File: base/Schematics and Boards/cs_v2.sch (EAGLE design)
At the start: 72 parts, among them J101 J-JTAG-CORTEX-NEEDLE6, J301 HIROSE-DF40_44-PIN_CONNECTORS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, J302 HIROSE-DF40_30-PIN_CONNECTORS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, Q201 FK3303010L, Q202 FK3303010L, Q203 FK3303010L, Q204 DMG3415UFY4Q-7, U1 AT25SF641-MHB-T, U101 ATSAMD51, U201 COULOMB-MAX17262, U202 CUS520H3F, U203 MAX77827BEWC+T, U204 SENSOR-SI7006, U205 LOADSWITCH-MIC94164, U206 LOADSWITCH-MIC94164, Y101 16M, Y102 ABS07-32.768KHZ-9-T

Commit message: Minor sh changes; placed compressed power subsys, gitignore temp files
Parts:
- added JP1: JUMPER-SMT_3_1-NC_PASTE_NO-SILK, SparkFun-Jumpers:JUMPER-SMT_3_1-NC_PASTE_NO-SILK
- added TP1, TP10, TP2, TP5, TP6, TP7, TP8, TP9: TPTP08R, TestPoints:TPTP08R
- C206, C208: SPICEPREFIX (none) -> C
- R208: SPICEPREFIX (none) -> R
- U205: SPICEPREFIX (none) -> E
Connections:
- net N$18 renamed +3V3_DTR_SENSE
- net N$19 renamed +3V3_PROC_SENSE
- new net VDD_SW_IN: JP1.2, S201.P
- net +3V3_DTR: now also TP6.TP
- net +3V3_PROC: now also TP5.TP
- net +3V3_STOR: now also TP8.TP
- net +3V3_TEMP: now also TP7.TP
- net +3V7_BATT: now also JP1.1
- net CC_IN: now also S201.S; no longer S201.O
- net DTR_MASTER_I2C_SCL: now also TP10.TP
- net DTR_MASTER_I2C_SDA: now also TP9.TP
- net N$1: now also TP1.TP
- net VDD_SW: now also JP1.3; no longer S201.P
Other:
- note added: "Provide info on board health (humitidy/temp) and info to help with crystal frequency offset resulting from temperature; should be placed near XTALs"
- note removed: "Idea: put similar pins (rather than SERCOM buses) right next to each other to make passthrough easier for dtr boards"
- note removed: "Provide info on board health (humitidy/temp) and info to help with crystal frequency offset resulting from temperature"
- moved on the sheet: C201, C203, S201, U201, U202

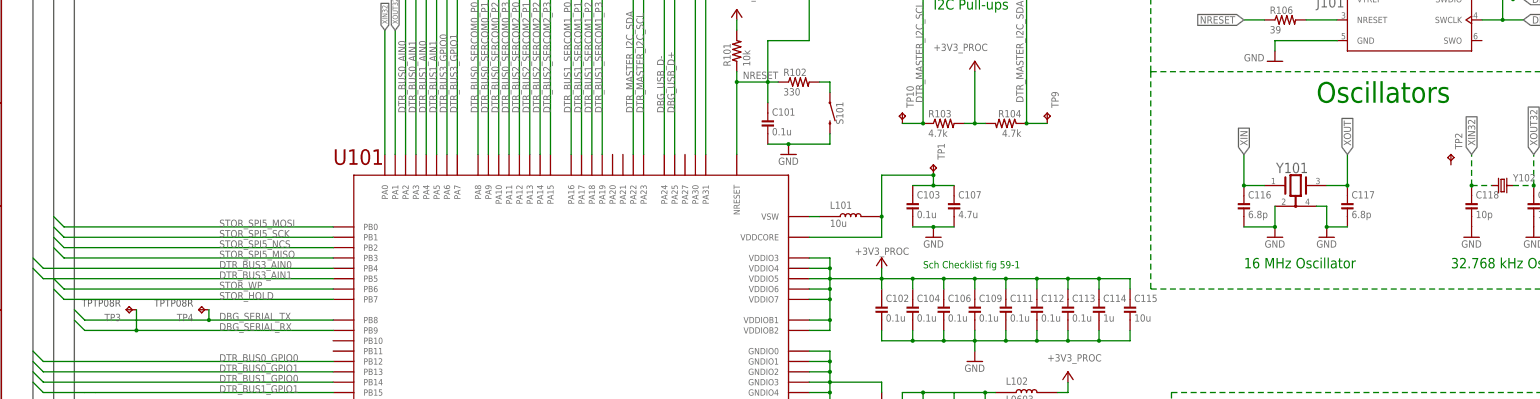
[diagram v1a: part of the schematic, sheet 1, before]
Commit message: Board placement for 1in x 1in. Unrouted
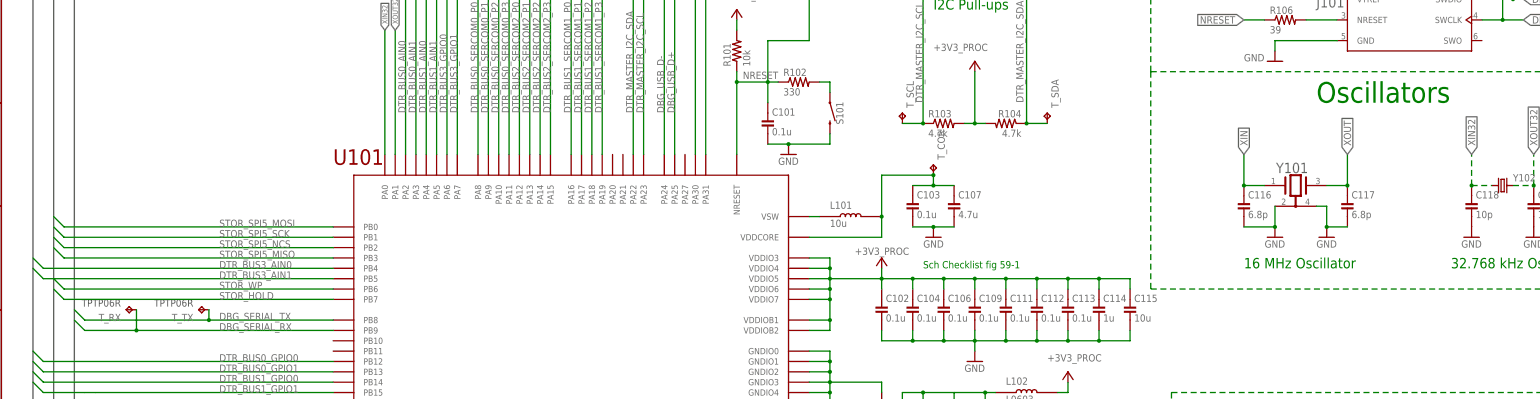
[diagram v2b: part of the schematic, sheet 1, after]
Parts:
- removed TP1, TP10, TP2, TP3, TP4, TP5, TP6, TP7, TP8, TP9: TPTP08R, TestPoints:TPTP08R
- added T_COR, T_CPU, T_DTR, T_RX, T_SCL, T_SDA, T_STR, T_TMP, T_TX: TPTP06R, TestPoints:TPTP06R
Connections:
- net N$2 renamed VSW
- net N$3 renamed VDDANA
- removed net N$1: C103.1, C107.1, L101.2, TP1.TP, U101.VDDCORE
- new net VDDCORE: C103.1, C107.1, L101.2, T_COR.TP, U101.VDDCORE
- net +3V3_DTR: now also T_DTR.TP; no longer TP6.TP
- net +3V3_PROC: now also T_CPU.TP; no longer TP5.TP
- net +3V3_STOR: now also T_STR.TP; no longer TP8.TP
- net +3V3_TEMP: now also T_TMP.TP; no longer TP7.TP
- net DBG_SERIAL_RX: now also T_RX.TP; no longer TP3.TP
- net DBG_SERIAL_TX: now also T_TX.TP; no longer TP4.TP
- net DTR_MASTER_I2C_SCL: now also T_SCL.TP; no longer TP10.TP
- net DTR_MASTER_I2C_SDA: now also T_SDA.TP; no longer TP9.TP
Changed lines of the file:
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@@
 <part name="+3V5" library="Supplies" deviceset="+3V3" device=""/>
 <part name="GND18" library="Supplies" deviceset="GND" device=""/>
-<part name="TP3" library="TestPoints" deviceset="TP" device="TP08R" package3d_urn="urn:adsk.eagle:package:27956/1"/>
-<part name="TP4" library="TestPoints" deviceset="TP" device="TP08R" package3d_urn="urn:adsk.eagle:package:27956/1"/>
+<part name="T_RX" library="TestPoints" deviceset="TP" device="TP06R" package3d_urn="urn:adsk.eagle:package:27954/1" value="TPTP06R"/>
+<part name="T_TX" library="TestPoints" deviceset="TP" device="TP06R" package3d_urn="urn:adsk.eagle:package:27954/1" value="TPTP06R"/>
 <part name="R106" library="Resistors" deviceset="R-" device="0402" value="39">
 <attribute name="PART_NO" value="ERJ-2GEJ390X"/>
@@
 <part name="GND14" library="Supplies" deviceset="GND" device=""/>
 <part name="JP1" library="SparkFun-Jumpers" deviceset="JUMPER-SMT_3_1-NC_PASTE" device="_NO-SILK" package3d_urn="urn:adsk.eagle:package:39291/1"/>
-<part name="TP1" library="TestPoints" deviceset="TP" device="TP08R" package3d_urn="urn:adsk.eagle:package:27956/1"/>
-<part name="TP2" library="TestPoints" deviceset="TP" device="TP08R" package3d_urn="urn:adsk.eagle:package:27956/1"/>
-<part name="TP5" library="TestPoints" deviceset="TP" device="TP08R" package3d_urn="urn:adsk.eagle:package:27956/1"/>
-<part name="TP6" library="TestPoints" deviceset="TP" device="TP08R" package3d_urn="urn:adsk.eagle:package:27956/1"/>
-<part name="TP7" library="TestPoints" deviceset="TP" device="TP08R" package3d_urn="urn:adsk.eagle:package:27956/1"/>
-<part name="TP8" library="TestPoints" deviceset="TP" device="TP08R" package3d_urn="urn:adsk.eagle:package:27956/1">
+<part name="T_COR" library="TestPoints" deviceset="TP" device="TP06R" package3d_urn="urn:adsk.eagle:package:27954/1" value="TPTP06R"/>
+<part name="T_CPU" library="TestPoints" deviceset="TP" device="TP06R" package3d_urn="urn:adsk.eagle:package:27954/1" value="TPTP06R"/>
+<part name="T_DTR" library="TestPoints" deviceset="TP" device="TP06R" package3d_urn="urn:adsk.eagle:package:27954/1" value="TPTP06R"/>
+<part name="T_TMP" library="TestPoints" deviceset="TP" device="TP06R" package3d_urn="urn:adsk.eagle:package:27954/1" value="TPTP06R"/>
+<part name="T_STR" library="TestPoints" deviceset="TP" device="TP06R" package3d_urn="urn:adsk.eagle:package:27954/1" value="TPTP06R">
 <attribute name="SPICEPREFIX" value="X"/>
 </part>
-<part name="TP9" library="TestPoints" deviceset="TP" device="TP08R" package3d_urn="urn:adsk.eagle:package:27956/1"/>
-<part name="TP10" library="TestPoints" deviceset="TP" device="TP08R" package3d_urn="urn:adsk.eagle:package:27956/1"/>
+<part name="T_SDA" library="TestPoints" deviceset="TP" device="TP06R" package3d_urn="urn:adsk.eagle:package:27954/1" value="TPTP06R"/>
+<part name="T_SCL" library="TestPoints" deviceset="TP" device="TP06R" package3d_urn="urn:adsk.eagle:package:27954/1" value="TPTP06R"/>
 </parts>
 <sheets>
@@
 <attribute name="VALUE" x="307.34" y="213.36" size="1.778" layer="96"/>
 </instance>
-<instance part="TP3" gate="G$1" x="33.02" y="152.4" smashed="yes" rot="R90">
+<instance part="T_RX" gate="G$1" x="33.02" y="152.4" smashed="yes" rot="R90">
 <attribute name="NAME" x="31.75" y="151.384" size="1.778" layer="95" rot="R180"/>
 <attribute name="VALUE" x="31.75" y="154.94" size="1.778" layer="97" rot="R180"/>
 </instance>
-<instance part="TP4" gate="G$1" x="50.8" y="152.4" smashed="yes" rot="R90">
+<instance part="T_TX" gate="G$1" x="50.8" y="152.4" smashed="yes" rot="R90">
 <attribute name="NAME" x="49.53" y="151.384" size="1.778" layer="95" rot="R180"/>
 <attribute name="VALUE" x="49.53" y="154.94" size="1.778" layer="97" rot="R180"/>
@@
 <attribute name="VALUE" x="363.22" y="63.5" size="1.778" layer="96"/>
 </instance>
-<instance part="TP1" gate="G$1" x="231.14" y="187.96" smashed="yes" rot="MR0">
+<instance part="T_COR" gate="G$1" x="231.14" y="187.96" smashed="yes" rot="MR0">
 <attribute name="NAME" x="232.156" y="189.23" size="1.778" layer="95" rot="MR90"/>
 </instance>
-<instance part="TP2" gate="G$1" x="358.14" y="190.5" smashed="yes" rot="MR0">
-<attribute name="NAME" x="359.156" y="191.77" size="1.778" layer="95" rot="MR90"/>
-</instance>
-<instance part="TP9" gate="G$1" x="259.08" y="200.66" smashed="yes" rot="MR0">
+<instance part="T_SDA" gate="G$1" x="259.08" y="200.66" smashed="yes" rot="MR0">
 <attribute name="NAME" x="260.096" y="201.93" size="1.778" layer="95" rot="MR90"/>
 </instance>
-<instance part="TP10" gate="G$1" x="223.52" y="200.66" smashed="yes" rot="MR0">
+<instance part="T_SCL" gate="G$1" x="223.52" y="200.66" smashed="yes" rot="MR0">
 <attribute name="NAME" x="224.536" y="201.93" size="1.778" layer="95" rot="MR90"/>
 </instance>
@@
 </segment>
 </net>
-<net name="N$1" class="0">
+<net name="VDDCORE" class="0">
 <segment>
 <pinref part="U101" gate="G$1" pin="VDDCORE"/>
@@
 <wire x1="231.14" y1="185.42" x2="231.14" y2="182.88" width="0.1524" layer="91"/>
 <junction x="231.14" y="182.88"/>
-<pinref part="TP1" gate="G$1" pin="TP"/>
+<pinref part="T_COR" gate="G$1" pin="TP"/>
 <junction x="231.14" y="185.42"/>
 </segment>
 </net>
-<net name="N$2" class="0">
+<net name="VSW" class="0">
 <segment>
 <pinref part="U101" gate="G$1" pin="VSW"/>
@@
 </segment>
 </net>
-<net name="N$3" class="0">
+<net name="VDDANA" class="0">
 <segment>
 <pinref part="U101" gate="G$1" pin="VDDANA1"/>
@@
 <wire x1="53.34" y1="149.86" x2="22.86" y2="149.86" width="0.1524" layer="91"/>
 <wire x1="22.86" y1="149.86" x2="20.32" y2="152.4" width="0.1524" layer="91"/>
-<pinref part="TP4" gate="G$1" pin="TP"/>
+<pinref part="T_TX" gate="G$1" pin="TP"/>
 <wire x1="53.34" y1="149.86" x2="53.34" y2="152.4" width="0.1524" layer="91"/>
 <junction x="53.34" y="149.86"/>
@@
 <wire x1="35.56" y1="147.32" x2="22.86" y2="147.32" width="0.1524" layer="91"/>
 <wire x1="22.86" y1="147.32" x2="20.32" y2="149.86" width="0.1524" layer="91"/>
-<pinref part="TP3" gate="G$1" pin="TP"/>
+<pinref part="T_RX" gate="G$1" pin="TP"/>
 <wire x1="35.56" y1="147.32" x2="35.56" y2="152.4" width="0.1524" layer="91"/>
 <junction x="35.56" y="147.32"/>
@@
 <wire x1="254" y1="198.12" x2="259.08" y2="198.12" width="0.1524" layer="91"/>
 <junction x="254" y="198.12"/>
-<pinref part="TP9" gate="G$1" pin="TP"/>
+<pinref part="T_SDA" gate="G$1" pin="TP"/>
 </segment>
 </net>
@@
 <pinref part="R103" gate="G$1" pin="1"/>
 <label x="228.6" y="203.2" size="1.778" layer="95" rot="R90"/>
-<pinref part="TP10" gate="G$1" pin="TP"/>
+<pinref part="T_SCL" gate="G$1" pin="TP"/>
 <wire x1="228.6" y1="198.12" x2="223.52" y2="198.12" width="0.1524" layer="91"/>
 <junction x="228.6" y="198.12"/>
@@
 <attribute name="NAME" x="86.36" y="175.641" size="1.778" layer="95" font="vector" rot="MR0"/>
 </instance>
-<instance part="TP5" gate="G$1" x="350.52" y="190.5" smashed="yes" rot="MR0">
+<instance part="T_CPU" gate="G$1" x="350.52" y="190.5" smashed="yes" rot="MR0">
 <attribute name="NAME" x="351.536" y="191.77" size="1.778" layer="95" rot="MR90"/>
 </instance>
-<instance part="TP6" gate="G$1" x="350.52" y="177.8" smashed="yes" rot="MR0">
+<instance part="T_DTR" gate="G$1" x="350.52" y="177.8" smashed="yes" rot="MR0">
 <attribute name="NAME" x="351.536" y="179.07" size="1.778" layer="95" rot="MR90"/>
 </instance>
-<instance part="TP7" gate="G$1" x="373.38" y="111.76" smashed="yes" rot="MR0">
+<instance part="T_TMP" gate="G$1" x="373.38" y="111.76" smashed="yes" rot="MR0">
 <attribute name="NAME" x="374.396" y="113.03" size="1.778" layer="95" rot="MR90"/>
 </instance>
-<instance part="TP8" gate="G$1" x="373.38" y="152.4" smashed="yes" rot="MR0">
+<instance part="T_STR" gate="G$1" x="373.38" y="152.4" smashed="yes" rot="MR0">
 <attribute name="NAME" x="374.396" y="153.67" size="1.778" layer="95" rot="MR90"/>
 </instance>
@@
 <wire x1="373.38" y1="149.86" x2="383.54" y2="149.86" width="0.1524" layer="91"/>
 <wire x1="383.54" y1="149.86" x2="386.08" y2="152.4" width="0.1524" layer="91"/>
-<pinref part="TP8" gate="G$1" pin="TP"/>
+<pinref part="T_STR" gate="G$1" pin="TP"/>
 <junction x="373.38" y="149.86"/>
 </segment>
@@
 <wire x1="383.54" y1="175.26" x2="386.08" y2="177.8" width="0.1524" layer="91"/>
 <pinref part="JP204" gate="G$1" pin="1"/>
-<pinref part="TP6" gate="G$1" pin="TP"/>
+<pinref part="T_DTR" gate="G$1" pin="TP"/>
 <junction x="350.52" y="175.26"/>
 </segment>
@@
 <wire x1="383.54" y1="187.96" x2="386.08" y2="190.5" width="0.1524" layer="91"/>
 <pinref part="JP_PROC" gate="G$1" pin="1"/>
-<pinref part="TP5" gate="G$1" pin="TP"/>
+<pinref part="T_CPU" gate="G$1" pin="TP"/>
 <junction x="350.52" y="187.96"/>
 </segment>
@@
 <wire x1="373.38" y1="109.22" x2="383.54" y2="109.22" width="0.1524" layer="91"/>
 <wire x1="383.54" y1="109.22" x2="386.08" y2="111.76" width="0.1524" layer="91"/>
-<pinref part="TP7" gate="G$1" pin="TP"/>
+<pinref part="T_TMP" gate="G$1" pin="TP"/>
 <junction x="373.38" y="109.22"/>
 </segment>

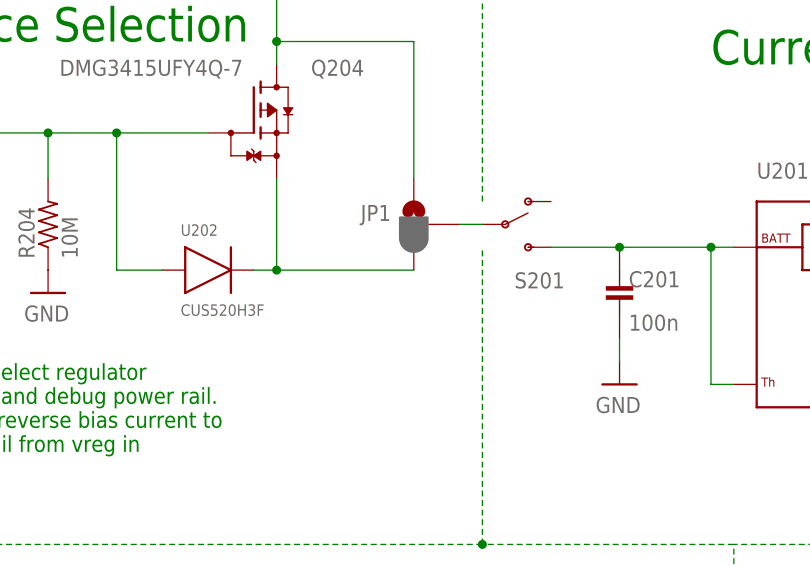
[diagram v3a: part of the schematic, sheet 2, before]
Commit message: Hand-route power traces and lock signals to prep for autoroute
Moved around some components to give more space for routing from processor to connectors

Hand routed all the power traces with 10mil traces. Should satisfy 6 mil separations, but design will need 5mils to escape all BGA signals. 

Locked traces and vias to prevent ripup from changing them
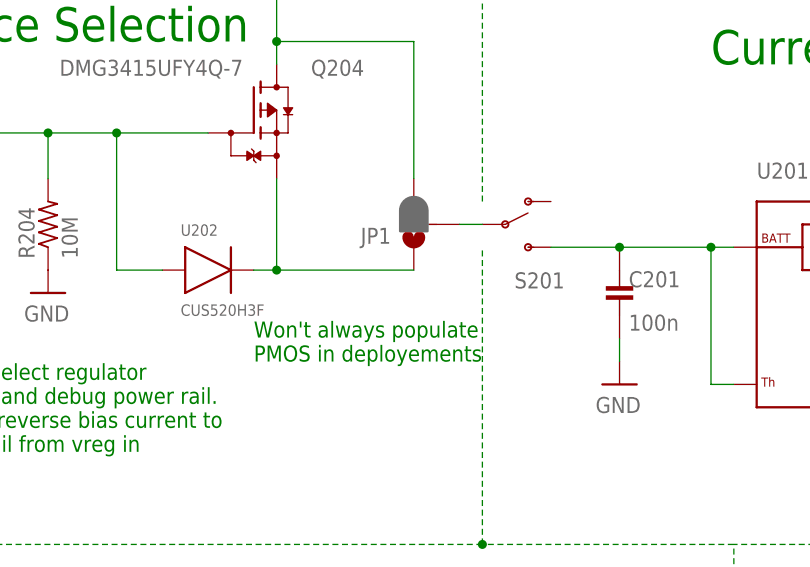
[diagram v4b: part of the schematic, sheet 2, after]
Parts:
- C114, C206, C207: device Capacitors:C-0603 -> Capacitors:C-0402; PART_NO C0603C105K8RACTU -> C0402C105M8PACTU; TC (none) -> X5R
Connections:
- removed net N$21: J302.1, J302.3, J302.5
- net +3V7_BATT: now also JP1.3; no longer JP1.1
- net GND: now also J302.1, J302.3, J302.5
- net VDD_SW: now also JP1.1; no longer JP1.3
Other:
- note added: "Won't always populate PMOS in deployements"
- moved on the sheet: JP1
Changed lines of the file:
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@@
 </part>
 <part name="+3V2" library="Supplies" deviceset="+3V3" device=""/>
-<part name="C114" library="Capacitors" deviceset="C-" device="0603" value="1u">
-<attribute name="PART_NO" value="C0603C105K8RACTU"/>
+<part name="C114" library="Capacitors" deviceset="C-" device="0402" value="1u">
+<attribute name="PART_NO" value="C0402C105M8PACTU"/>
+<attribute name="TC" value="X5R"/>
 <attribute name="VOLTAGE" value="10V"/>
 </part>
@@
 <attribute name="VOLTAGE" value="10V"/>
 </part>
-<part name="C206" library="Capacitors" deviceset="C-" device="0603" value="1u">
-<attribute name="PART_NO" value="C0603C105K8RACTU"/>
+<part name="C206" library="Capacitors" deviceset="C-" device="0402" value="1u">
+<attribute name="PART_NO" value="C0402C105M8PACTU"/>
 <attribute name="SPICEPREFIX" value="C"/>
+<attribute name="TC" value="X5R"/>
 <attribute name="VOLTAGE" value="10V"/>
 </part>
@@
 <attribute name="VOLTAGE" value="10V"/>
 </part>
-<part name="C207" library="Capacitors" deviceset="C-" device="0603" value="1u">
-<attribute name="PART_NO" value="C0603C105K8RACTU"/>
+<part name="C207" library="Capacitors" deviceset="C-" device="0402" value="1u">
+<attribute name="PART_NO" value="C0402C105M8PACTU"/>
+<attribute name="TC" value="X5R"/>
 <attribute name="VOLTAGE" value="10V"/>
 </part>
@@
 </busses>
 <nets>
-<net name="GND" class="1">
+<net name="GND" class="0">
 <segment>
 <pinref part="C107" gate="G$1" pin="2"/>
@@
 </segment>
 </net>
-<net name="+3V3_PROC" class="1">
+<net name="+3V3_PROC" class="0">
 <segment>
 <pinref part="U101" gate="G$1" pin="VDDIO3"/>
@@
 by not having the input directly
 connected to the battery?</text>
+<text x="71.12" y="160.02" size="1.778" layer="91">Won't always populate
+PMOS in deployements</text>
 </plain>
 <instances>
@@
 </instance>
 <instance part="+3V6" gate="G$1" x="248.92" y="48.26" smashed="yes"/>
-<instance part="JP1" gate="G$1" x="88.9" y="175.26" smashed="yes" rot="MR0">
-<attribute name="NAME" x="86.36" y="175.641" size="1.778" layer="95" font="vector" rot="MR0"/>
+<instance part="JP1" gate="G$1" x="88.9" y="175.26" smashed="yes" rot="R180">
+<attribute name="NAME" x="86.36" y="174.879" size="1.778" layer="95" font="vector" rot="R180"/>
 </instance>
 <instance part="T_CPU" gate="G$1" x="350.52" y="190.5" smashed="yes" rot="MR0">
@@
 </busses>
 <nets>
-<net name="GND" class="1">
+<net name="GND" class="0">
 <segment>
 <pinref part="GND11" gate="1" pin="GND"/>
@@
 </segment>
 </net>
-<net name="+3V3_PROC" class="1">
+<net name="+3V3_PROC" class="0">
 <segment>
 <label x="363.22" y="187.96" size="1.778" layer="95"/>
@@
 <wire x1="73.66" y1="195.58" x2="88.9" y2="195.58" width="0.1524" layer="91"/>
 <junction x="73.66" y="195.58"/>
-<pinref part="JP1" gate="G$1" pin="1"/>
+<pinref part="JP1" gate="G$1" pin="3"/>
 <wire x1="88.9" y1="195.58" x2="88.9" y2="180.34" width="0.1524" layer="91"/>
 </segment>
@@
 <pinref part="U202" gate="A" pin="N"/>
 <wire x1="71.12" y1="170.18" x2="73.66" y2="170.18" width="0.1524" layer="91"/>
+<pinref part="JP1" gate="G$1" pin="1"/>
+<wire x1="73.66" y1="170.18" x2="88.9" y2="170.18" width="0.1524" layer="91"/>
 <junction x="73.66" y="170.18"/>
-<pinref part="JP1" gate="G$1" pin="3"/>
-<wire x1="73.66" y1="170.18" x2="88.9" y2="170.18" width="0.1524" layer="91"/>
 </segment>
 </net>
@@
 </segment>
 </net>
-<net name="GND" class="1">
+<net name="GND" class="0">
 <segment>
 <wire x1="83.82" y1="132.08" x2="86.36" y2="132.08" width="0.1524" layer="91"/>
@@
 <pinref part="J301" gate="G$1" pin="5"/>
 </segment>
-</net>
-<net name="N$21" class="0">
 <segment>
 <wire x1="261.62" y1="139.7" x2="261.62" y2="129.54" width="0.1524" layer="91"/>
@@
 </segment>
 </net>
-<net name="+3V3_PROC" class="1">
+<net name="+3V3_PROC" class="0">
 <segment>
 <label x="274.32" y="177.8" size="1.778" layer="95" rot="R90"/>
